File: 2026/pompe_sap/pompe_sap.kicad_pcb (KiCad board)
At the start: 2 copper layers, 23 x 23 mm, 21 parts, among them J1 Conn_01x02_Pin, J2 22-03-5035, Q1 IRLML6344 (modèle du 6244), Q2 IRLML6344 (modèle du 6244), U2 NCP718xSN120, U3 INA180A1, U4 STM32L432KCUx

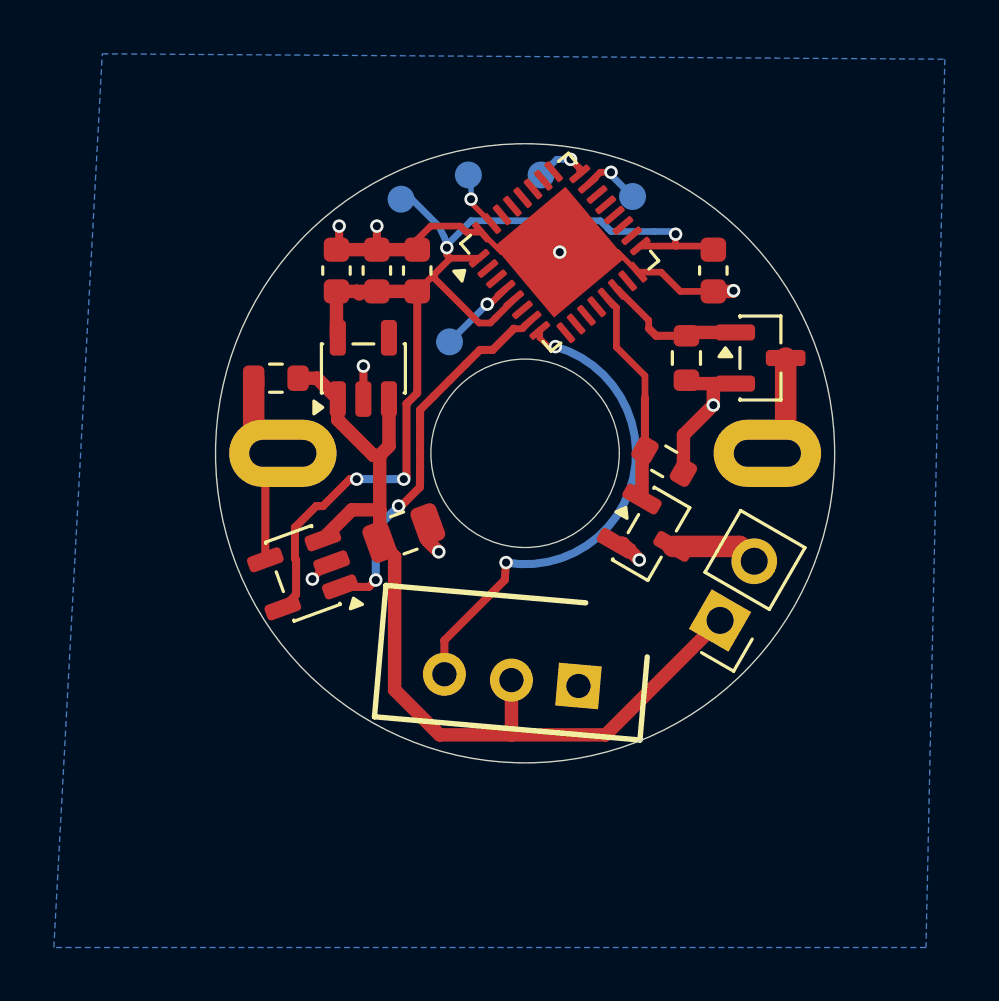
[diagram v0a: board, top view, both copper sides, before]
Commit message: [pompe SAP] Ajoute UART debug test points and LED.
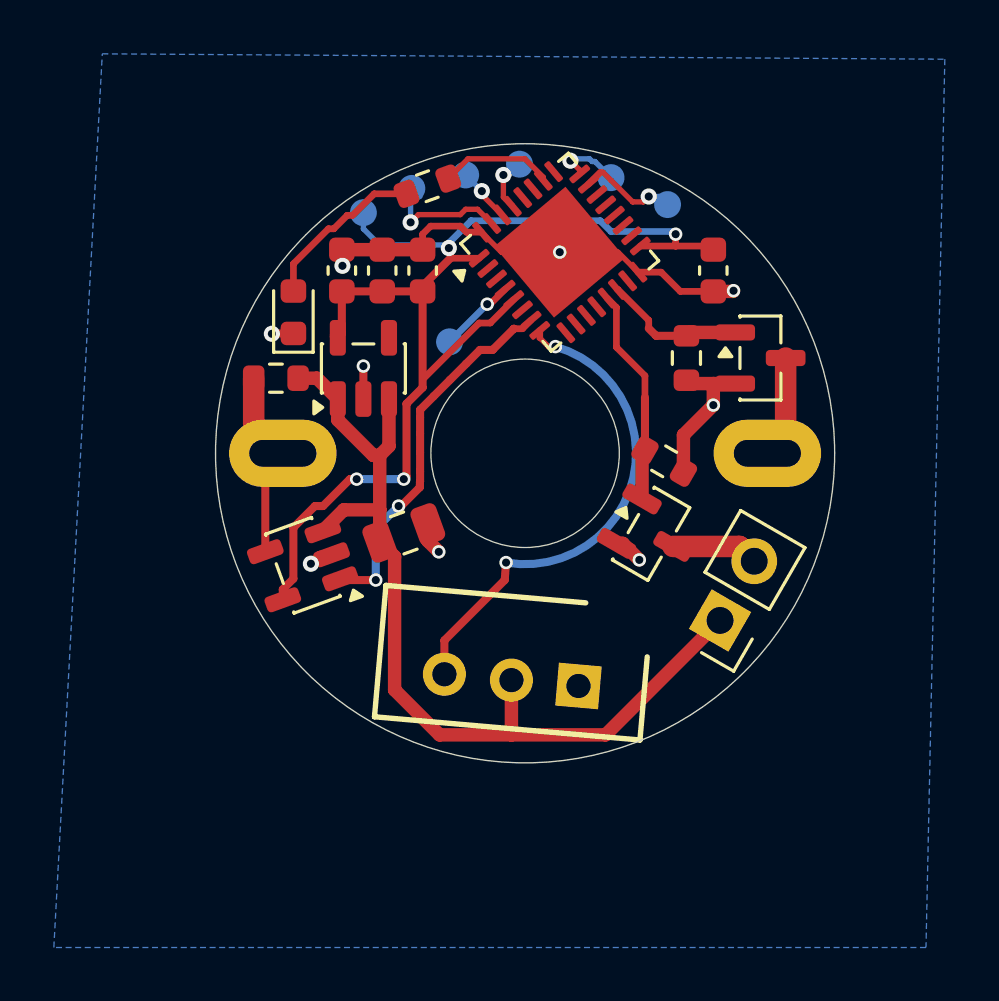
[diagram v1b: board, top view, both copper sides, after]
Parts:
- added D1: LED, LED_SMD:LED_0603_1608Metric, F.Cu at (140.9, 82.3)
- added R2: 390, Resistor_SMD:R_0603_1608Metric, F.Cu at (145.9, 77.6)
- added TP6: U1_TX, TestPoint:TestPoint_Pad_D1.0mm, B.Cu at (149.3, 76.8)
- added TP7: U1_RX, TestPoint:TestPoint_Pad_D1.0mm, B.Cu at (147.3, 77.2)
- moved TP2 2.60 mm to (152.7, 77.3)
- moved TP5 2.16 mm to (145.3, 77.7)
- moved TP4 1.49 mm to (143.5, 78.6)
- moved TP1 1.33 mm to (154.8, 78.3)
- moved U3 0.30 mm to (141.2, 91.7)
- moved C2 0.20 mm to (142.7, 80.8)
- moved C3 0.20 mm to (145.7, 80.8)
- moved C4 0.20 mm to (144.2, 80.8)
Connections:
- U4 pad 26: unconnected-(U4-PB3-Pad26) -> Net-(U4-PB3)
- U4 pad 29: unconnected-(U4-PB6-Pad29) -> Net-(U4-PB6)
- U4 pad 30: unconnected-(U4-PB7-Pad30) -> Net-(U4-PB7)
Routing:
- net Net-(D1-A): track 0.00 -> 6.29 mm
- net Net-(U4-PB3): track 0.00 -> 4.23 mm
- net /BOOT0: track 2.16 -> 5.14 mm
- net Net-(U4-PB6): track 0.00 -> 2.10 mm, vias 0 -> 1
- net Net-(U4-PB7): track 0.00 -> 2.04 mm, vias 0 -> 1
- net +3V3: track 42.4 -> 44.4 mm
- net /SWDIO: track 2.26 -> 3.79 mm
- net GND: track 28.2 -> 27.7 mm
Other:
- board text added: "RX"
- board text added: "TX"
